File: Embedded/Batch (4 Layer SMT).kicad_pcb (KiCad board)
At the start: 4 copper layers, 100 x 100 mm, 91 parts, among them J1 10171746-00021LF, J2 MicroSD, J2 PWR Jumper Pins, J3 L0 JST, J4 L1 JST, J5 5Vout, J6 A JST, J7 S Pins A, J8 S Pins B, J9 GNDout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

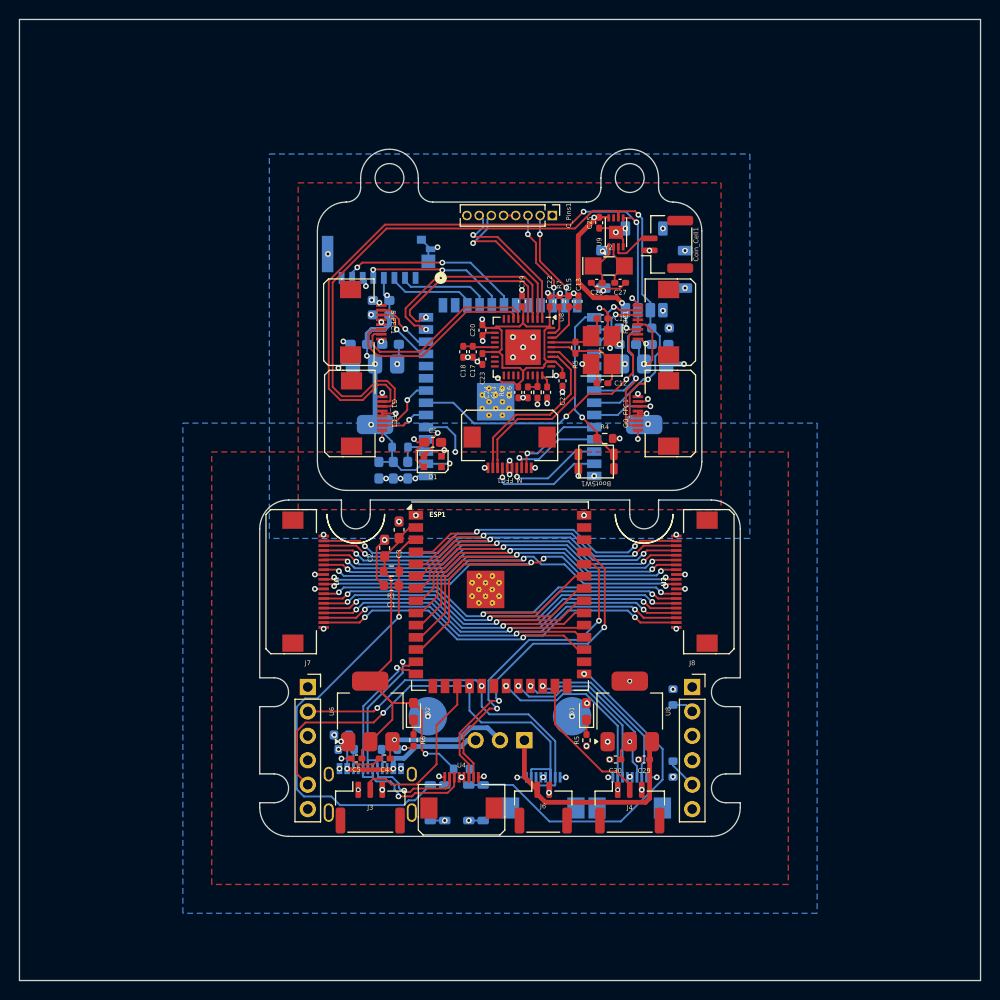
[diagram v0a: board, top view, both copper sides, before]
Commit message: Modified Board positions for optimal cutting & manufacture
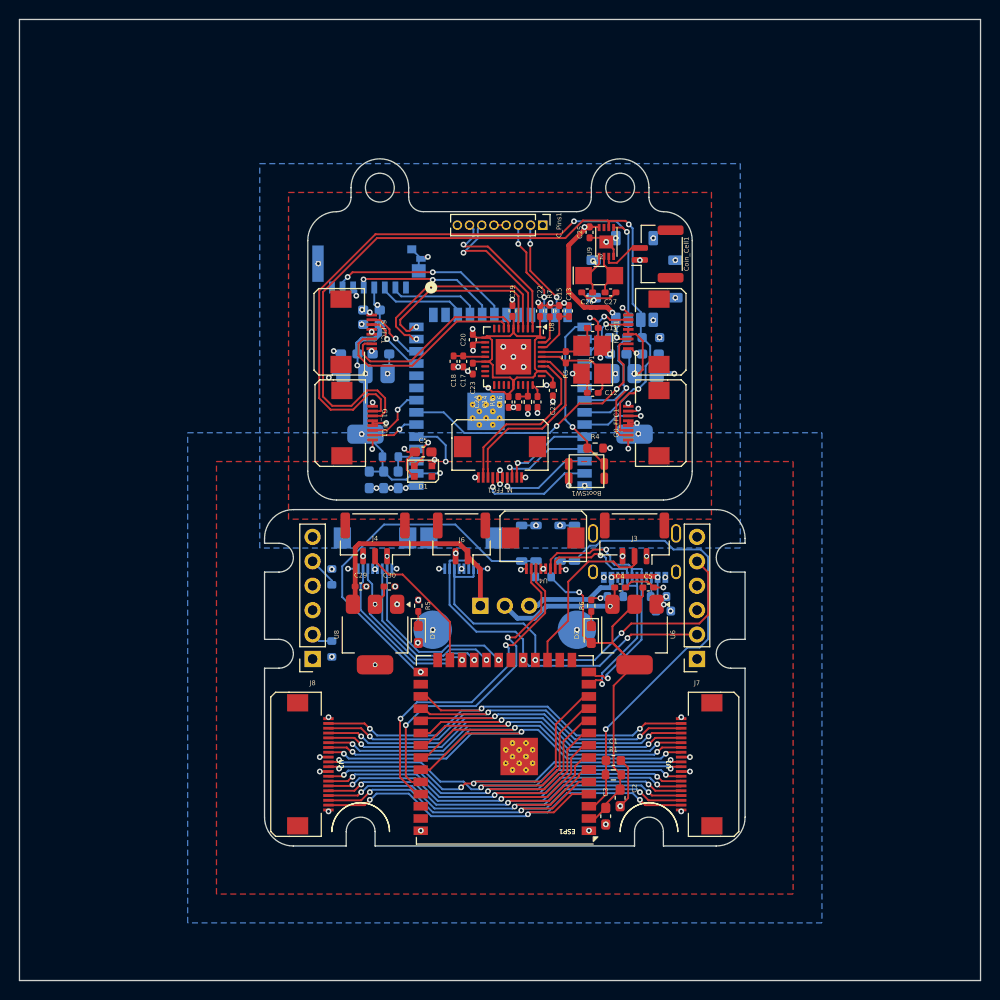
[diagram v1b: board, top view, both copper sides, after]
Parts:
- moved U1 42.9 mm to (99.5, 107.5), turned to 90 degrees
- moved U2 42.0 mm to (61.5, 107.5), turned to -90 degrees
- moved R7 40.7 mm to (62.5, 88.0), turned to 90 degrees
- moved J7 40.6 mm to (100.5, 96.5), turned to 180 degrees
- moved J1 40.0 mm to (94.0, 83.5), turned to 0 degrees
- moved J8 39.6 mm to (60.5, 96.5), turned to 180 degrees
- moved J3 39.2 mm to (94.0, 84.0), turned to 180 degrees
- moved J4 38.6 mm to (67.0, 84.0), turned to 180 degrees
- moved C3 36.7 mm to (91.0, 112.9), turned to -90 degrees
- moved R3 36.2 mm to (96.5, 90.0), turned to 0 degrees
- moved C6 35.9 mm to (97.0, 91.5), turned to 0 degrees
- moved R8 35.9 mm to (62.5, 95.5), turned to -90 degrees
- moved C2 35.7 mm to (92.5, 111.0), turned to -90 degrees
- moved C5 35.2 mm to (95.4, 89.1), turned to 0 degrees
- moved U3 35.1 mm to (67.0, 86.5), turned to 0 degrees
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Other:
- outline, holes or cut-outs redrawn
